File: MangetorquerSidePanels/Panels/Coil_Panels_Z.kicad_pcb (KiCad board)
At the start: 6 copper layers, 97 x 97.3 mm, 15 parts, among them J1 Through_Hole_1, J2 MOLEX_2053380006

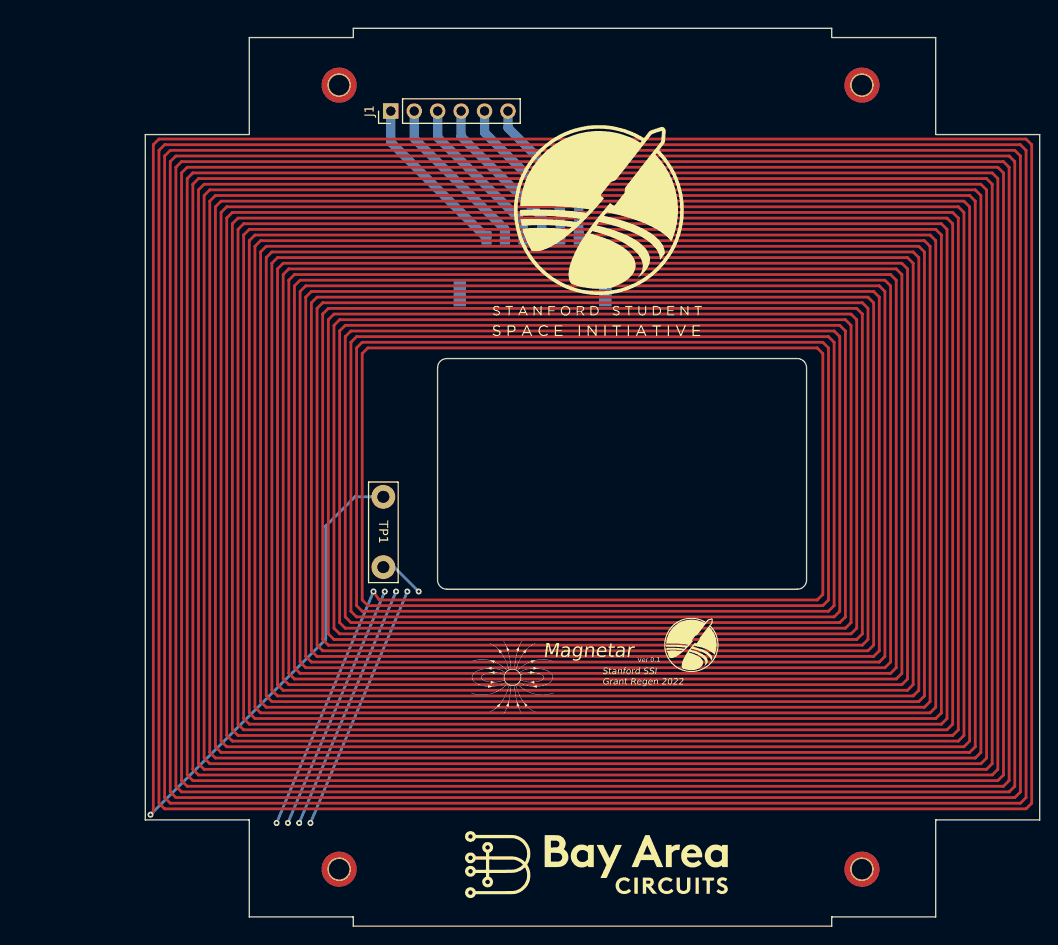
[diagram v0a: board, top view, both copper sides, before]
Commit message: Final flight side panels w/ magnetorquers finished, note final board thickness of 0.031'' and updated copper weight of 0.5oz for internal layers
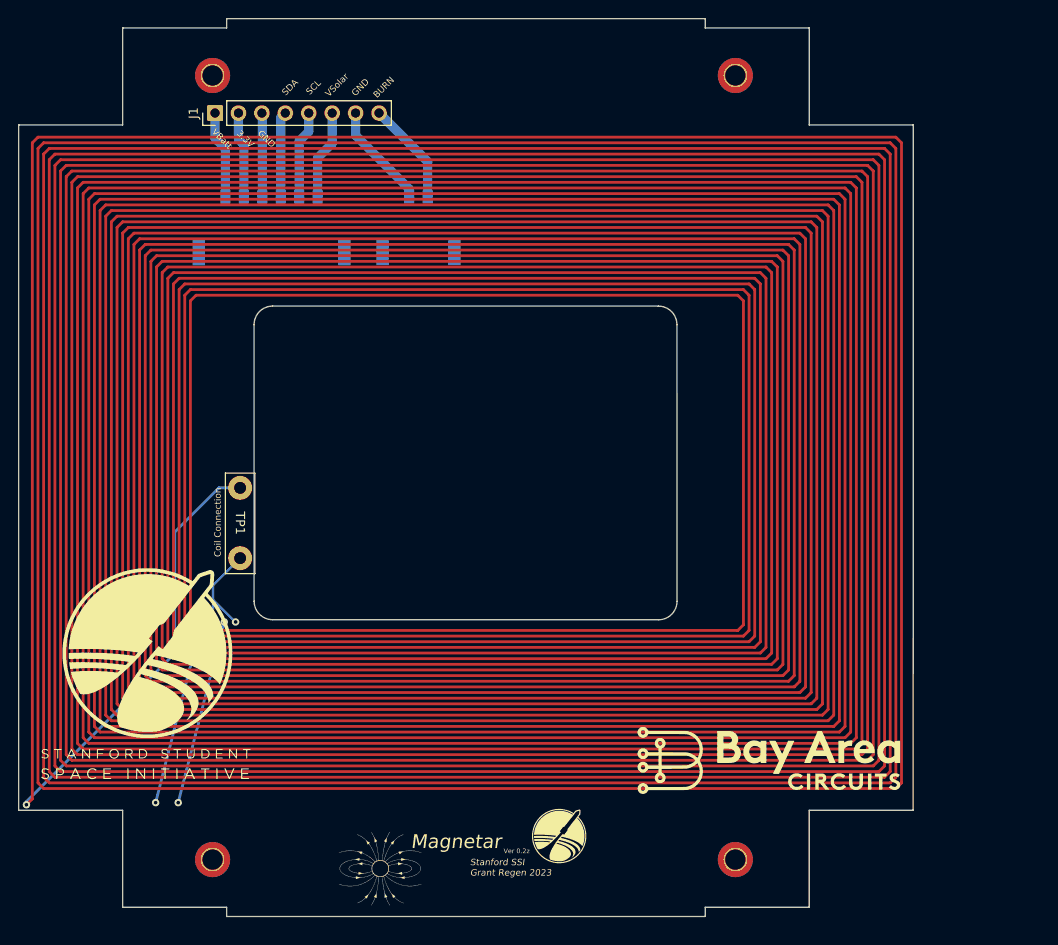
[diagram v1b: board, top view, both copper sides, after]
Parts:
- added J3: Conn_01x02, panels:2053380002, B.Cu at (129.3, 63.7)
- added REF**: logo_SSI_small, panels:logo_SSI_small, B.Cu at (150.9, 63.3)
- J1: value Through_Hole_1 -> Screw_Terminal_01x08; footprint Connector_PinHeader_2.54mm:PinHeader_1x06_P2.54mm_Vertical -> Connector_PinHeader_2.54mm:PinHeader_1x08_P2.54mm_Vertical
- moved H4 111.2 mm to (106.0, 50.5)
- moved H2 94.3 mm to (162.7, 135.5)
- moved REF** 68.6 mm to (99.1, 113.8)
- moved REF** 68.1 mm to (97.6, 81.8)
- moved REF** 29.3 mm to (171.0, 93.6), turned to 90 degrees
- moved J2 28.6 mm to (112.4, 67.2)
- moved REF** 25.2 mm to (142.5, 135.1)
- moved REF** 25.2 mm to (124.2, 136.5)
- moved REF** 25.2 mm to (143.4, 133.2)
- moved REF** 25.2 mm to (123.2, 131.9)
- moved REF** 21.8 mm to (166.5, 124.3)
- moved J1 19.1 mm to (106.3, 54.6)
- moved TP1 15.6 mm to (108.5, 99.0)
- moved H1 13.8 mm to (106.0, 135.5)
- moved H3 13.8 mm to (162.7, 50.5)
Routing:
- net Coil_IN: track 46506.2 -> 30247.5 mm, vias 10 -> 7
- net Net-(J1-Pad7): track 0.00 -> 11.5 mm
- net Net-(J3-Pad1): track 0.00 -> 11.3 mm
- net Net-(J2-Pad4): track 17.6 -> 9.11 mm
- net Net-(J2-Pad6): track 18.0 -> 9.56 mm
- net Net-(J2-Pad5): track 17.8 -> 9.40 mm
- net Net-(J2-Pad3): track 17.4 -> 9.30 mm
- net Net-(J2-Pad2): track 17.2 -> 9.52 mm
- net Net-(J2-Pad1): track 16.9 -> 9.75 mm
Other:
- outline, holes or cut-outs redrawn
- board text added: "!DO NOT DRIVE COILS OVER 3V!"
- board text added: "2023"
- board text added: "BURN"
- board text added: "Coil Connection"
- board text added: "Giganteum"
- board text added: "Sapling"
- board text added: "Stanford SSI Grant Regen 2023"
- board text added: "VBatt"
- board text added: "VSolar"
- board text added: "Ver 0.2z"
- board text added: "With thanks to my family, The Porteouses, Elizabeth, Will, and George And to my friends, Claudia, Holland, Katharine, Lyle, Parker, and Sofia Love, Iso"
- board text removed: "GR+IB"
- board text removed: "Stanford SSI Grant Regen 2022"
- board text removed: "VBATT"
- board text removed: "VSOLAR"
- board text removed: "Ver 0.1"

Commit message: added magnetorquers
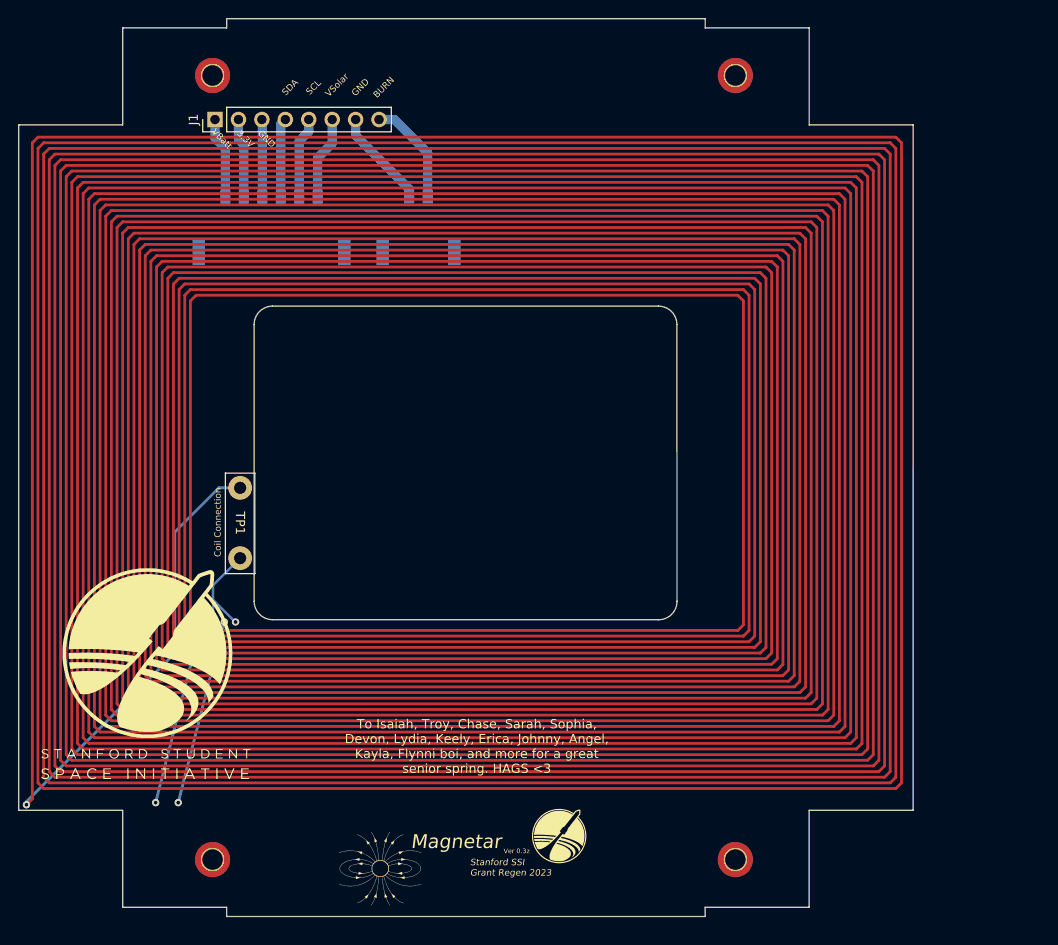
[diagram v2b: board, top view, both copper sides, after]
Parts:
- removed the REF** at (166.5, 124.3)
- moved J1 0.70 mm to (106.3, 55.3)
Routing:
- net Net-(J2-Pad6): track 9.56 -> 8.86 mm
- net Net-(J2-Pad5): track 9.40 -> 8.70 mm
- net Net-(J2-Pad4): track 9.11 -> 8.41 mm
- net Net-(J2-Pad3): track 9.30 -> 8.60 mm
- net Net-(J2-Pad2): track 9.52 -> 8.82 mm
- net Net-(J2-Pad1): track 9.75 -> 9.05 mm
- net Net-(J1-Pad7): track 11.5 -> 10.8 mm
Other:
- board text added: "Magnifica"
- board text added: "To Isaiah, Troy, Chase, Sarah, Sophia, Devon, Lydia, Keely, Erica, Johnny, Angel, Kayla, Flynni boi, and more for a great senior spring. HAGS <3"
- board text added: "Ver 0.3z"
- board text removed: "Giganteum"
- board text removed: "Ver 0.2z"
